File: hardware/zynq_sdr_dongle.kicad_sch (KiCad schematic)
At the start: 19 parts, among them J10 Conn_01x13_Male, J11 Conn_01x16_Male

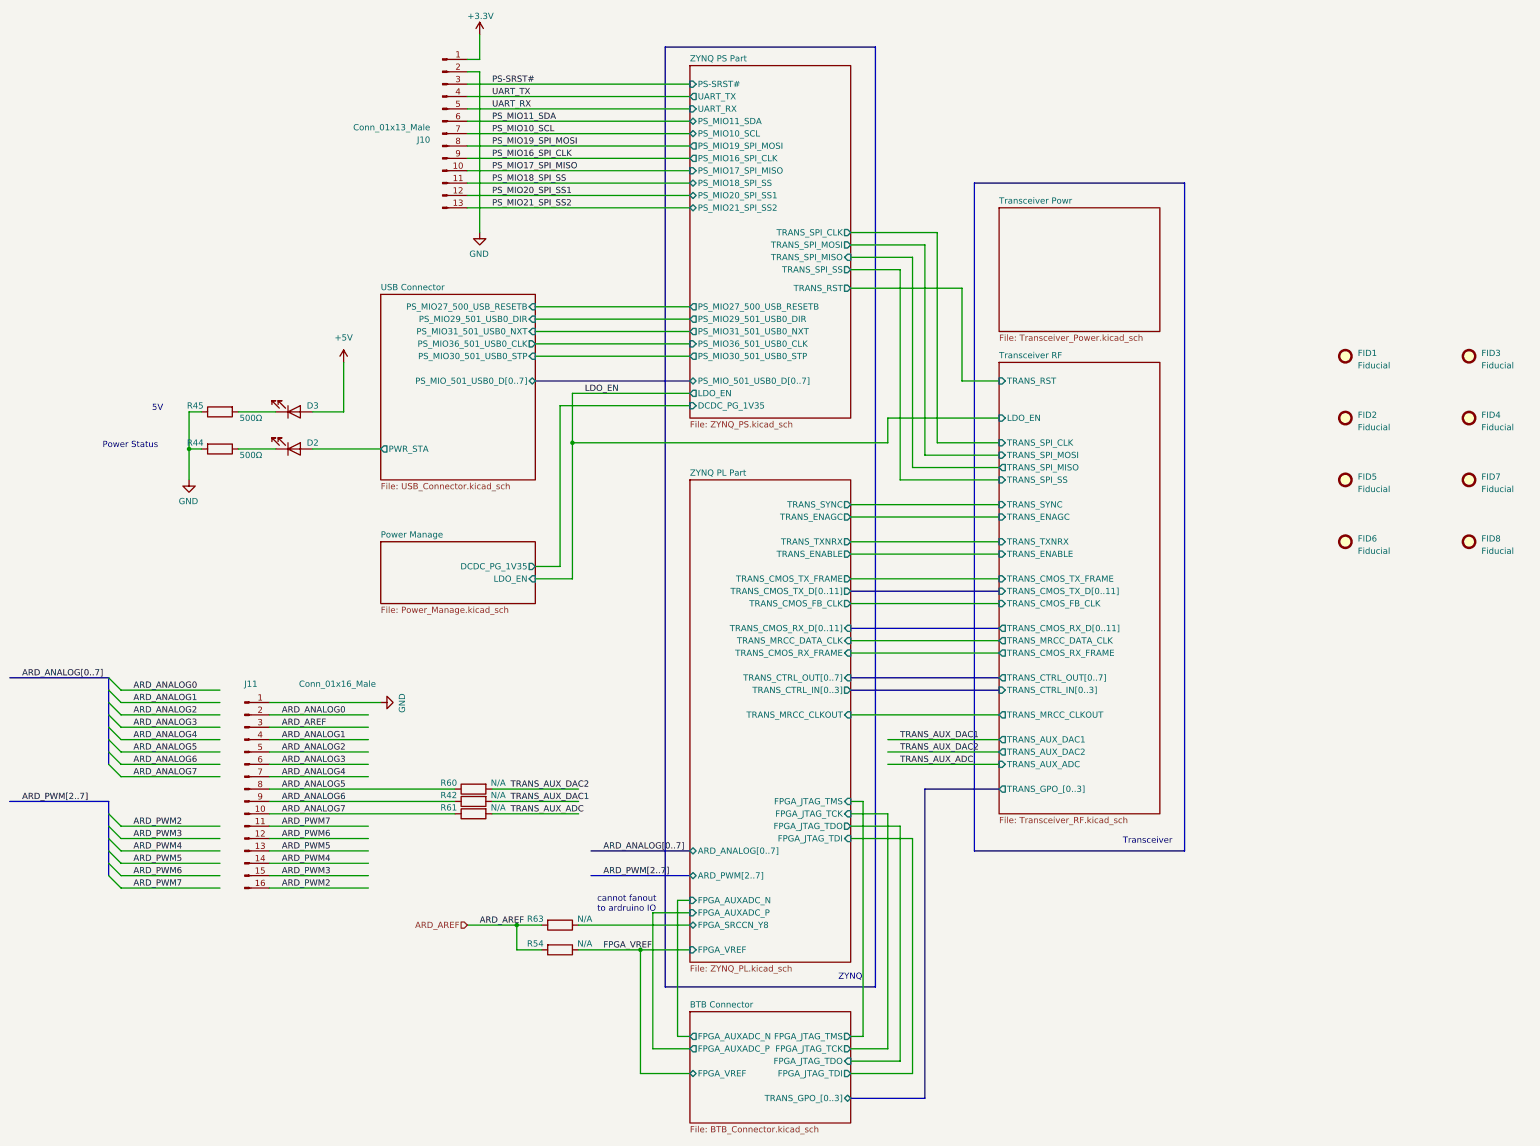
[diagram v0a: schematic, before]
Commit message: delete RF transceiver
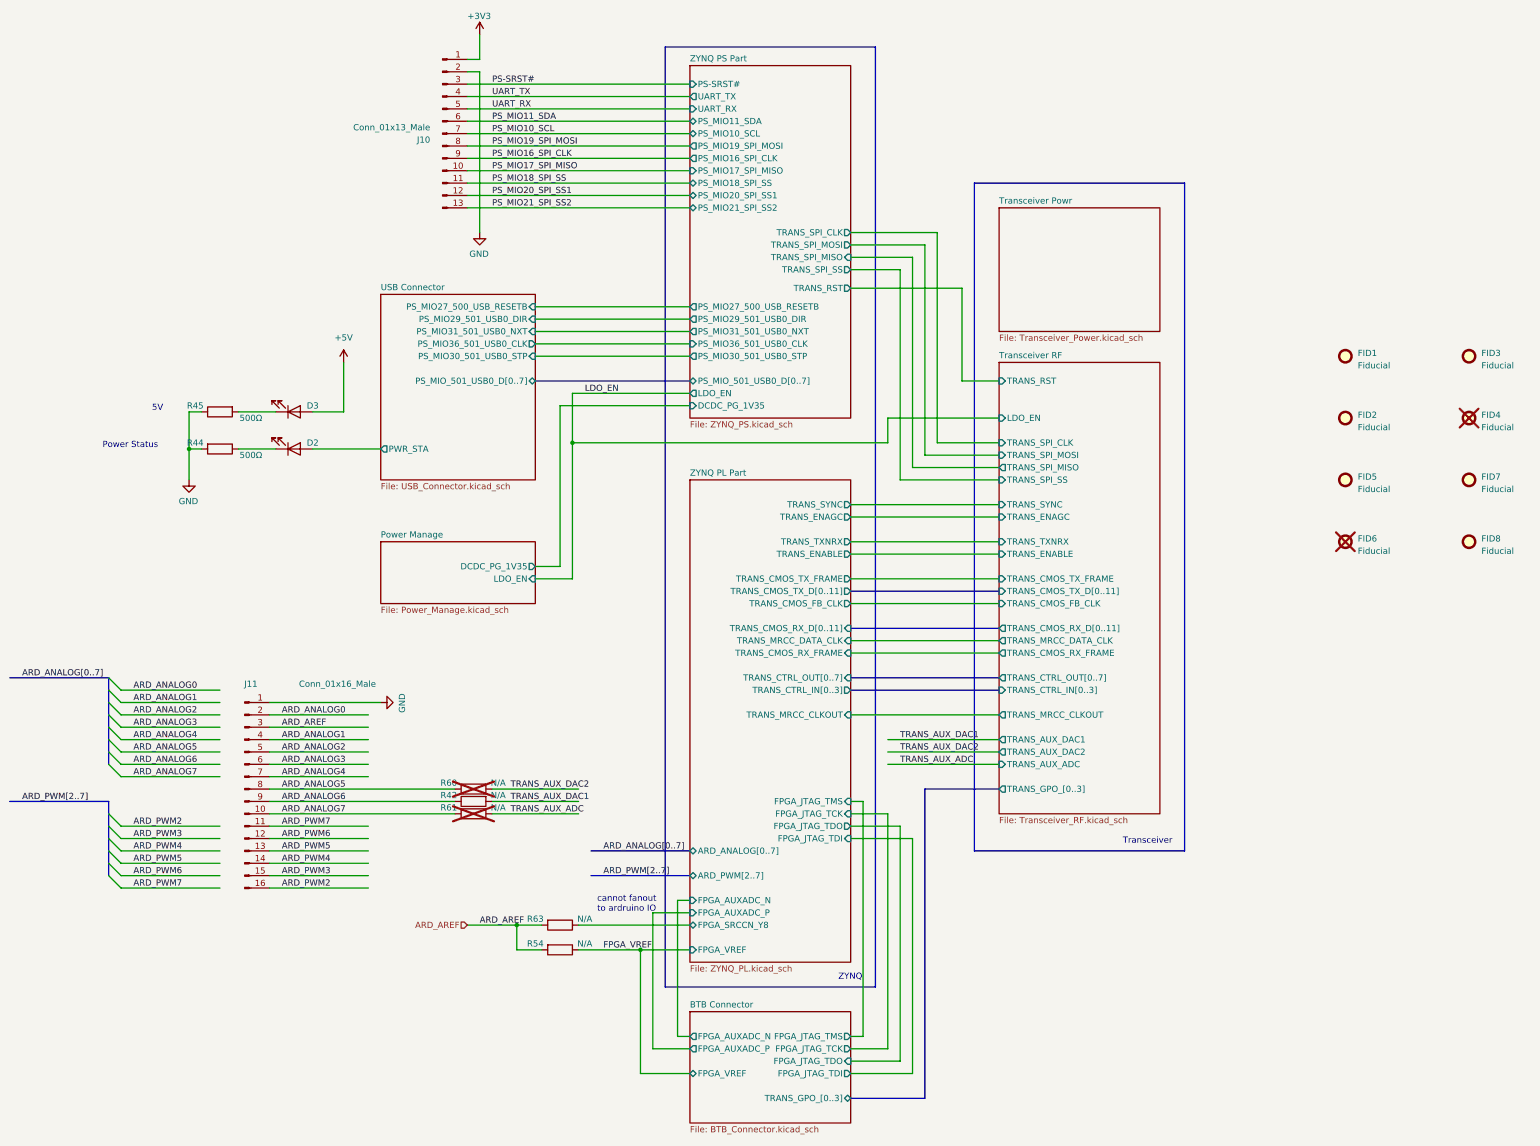
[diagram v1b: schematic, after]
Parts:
- FID4, FID6, R60, R61: now not fitted
